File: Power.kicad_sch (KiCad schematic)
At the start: 9 parts, among them U1 CN3063, U3 TPS7A0522PDBV

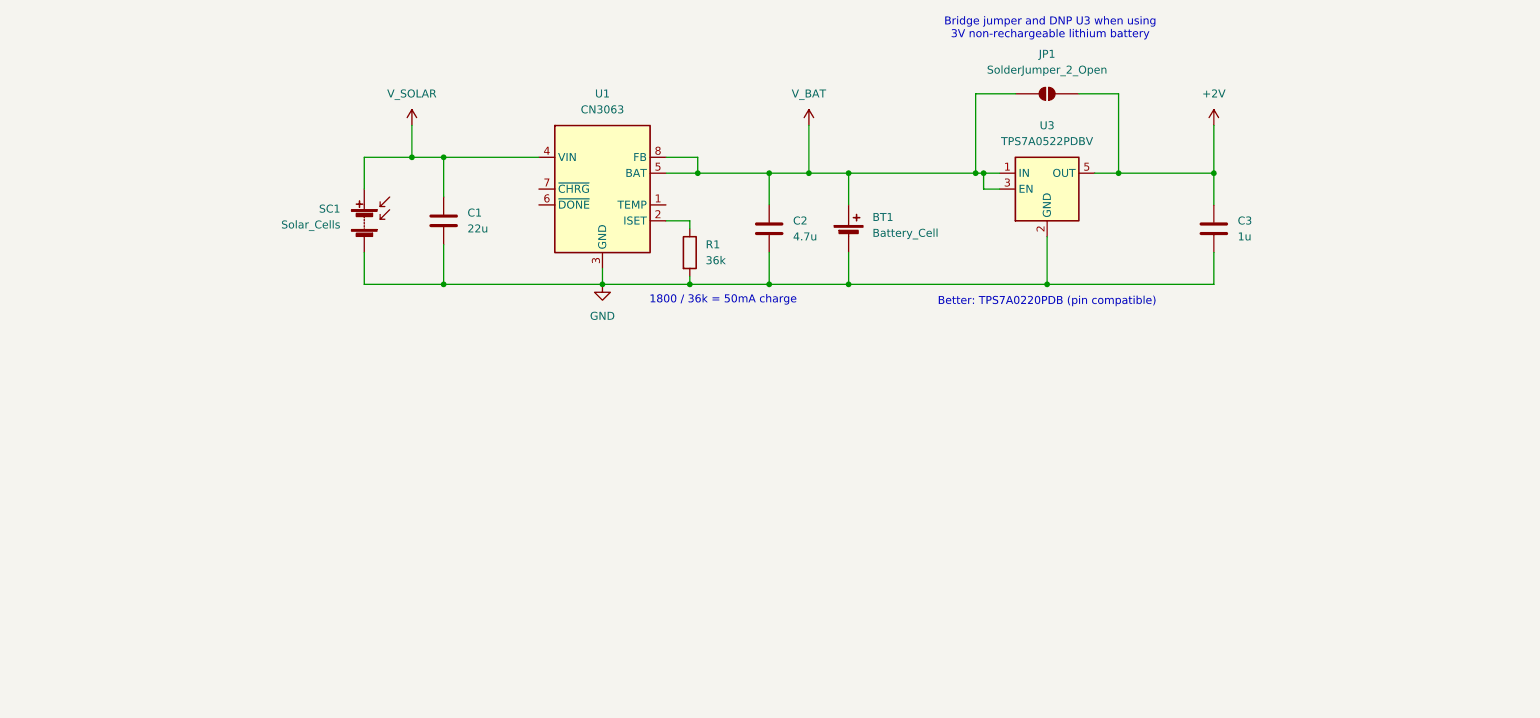
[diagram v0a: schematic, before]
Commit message: add initial pinouts and USB
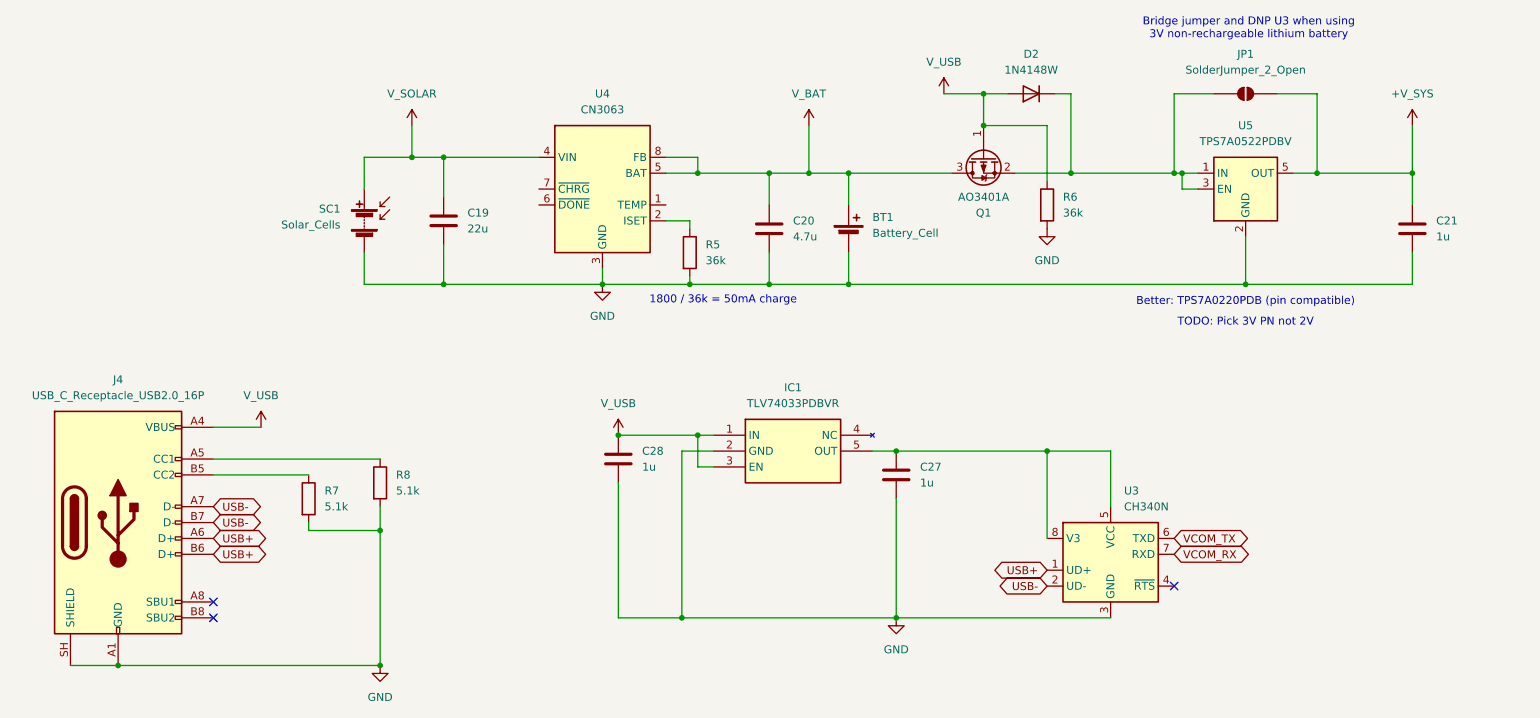
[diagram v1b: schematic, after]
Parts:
- added C27, C28: 1u, Capacitor_SMD:C_0805_2012Metric_Pad1.18x1.45mm_HandSolder, symbol Device:C
- added D2: 1N4148W, Diode_SMD:D_SOD-123, symbol Diode:1N4148W
- added IC1: TLV74033PDBVR, SOT95P280X145-5N, symbol SamacSys_Parts:TLV74033PDBVR
- added J4: USB_C_Receptacle_USB2.0_16P, symbol Connector:USB_C_Receptacle_USB2.0_16P
- added Q1: AO3401A, Package_TO_SOT_SMD:SOT-23, symbol Transistor_FET:AO3401A
- added R6: 36k, Resistor_SMD:R_0603_1608Metric_Pad0.98x0.95mm_HandSolder, symbol Device:R
- added R7, R8: 5.1k, Resistor_SMD:R_0603_1608Metric_Pad0.98x0.95mm_HandSolder, symbol Device:R
- added U3: CH340N, Package_SO:JEITA_SOIC-8_3.9x4.9mm_P1.27mm, symbol Interface_USB:CH340N
- renumbered C1 to C19, C2 to C20, C3 to C21, R1 to R5, U1 to U4, U3 to U5
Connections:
- net GND: now also C27.2, C28.2, IC1.2 (GND), J4.A1 (GND), J4.A12 (GND), J4.B1 (GND), J4.B12 (GND), J4.SH (SHIELD), R6.2, R7.2, R8.2, U3.3 (GND)
- net V_BAT: now also Q1.3 (D); no longer JP1.1 (A), U5.1 (IN), U5.3 (EN)
- net +2V renamed +V_SYS
- new net: C27.1, IC1.5 (OUT), U3.5 (VCC), U3.8 (V3)
- new net: J4.B5 (CC2), R7.1
- new net: D2.1 (K), JP1.1 (A), Q1.2 (S), U5.1 (IN), U5.3 (EN)
- new net: J4.A5 (CC1), R8.1
- new net USB+: J4.A6 (D+), J4.B6 (D+), U3.1 (UD+)
- new net USB-: J4.A7 (D-), J4.B7 (D-), U3.2 (UD-)
- new net VCOM_RX: U3.7 (RXD)
- new net VCOM_TX: U3.6 (TXD)
- new net V_USB: C28.1, D2.2 (A), IC1.1 (IN), IC1.3 (EN), J4.A4 (VBUS), J4.A9 (VBUS), J4.B4 (VBUS), J4.B9 (VBUS), Q1.1 (G), R6.1
- no-connect marks 0 -> 3
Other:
- note added: "TODO: Pick 3V PN not 2V"
- moved on the sheet: C21, JP1, U5

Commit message: add IO ports, begin layout
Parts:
- J4: footprint (none) -> Connector_USB:USB_C_Receptacle_GCT_USB4105-xx-A_16P_TopMnt_Horizontal
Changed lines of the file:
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@@
 			)
 		)
-		(property "Footprint" ""
+		(property "Footprint" "Connector_USB:USB_C_Receptacle_GCT_USB4105-xx-A_16P_TopMnt_Horizontal"
 			(at 49.53 127 0)
 			(hide yes)
@@
 			(at 45.72 127 0)
 			(hide yes)
+			(show_name no)
+			(do_not_autoplace no)
+			(effects
+				(font
+					(size 1.27 1.27)
+				)
+			)
+		)
+		(property "Field5" ""
+			(at 45.72 127 0)
+			(hide yes)

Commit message: minor schematic changes
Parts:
- C21, C27, C28: footprint Capacitor_SMD:C_0805_2012Metric_Pad1.18x1.45mm_HandSolder -> Capacitor_SMD:C_0603_1608Metric_Pad1.08x0.95mm_HandSolder
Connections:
- net V_USB: now also C27.1; no longer C28.1
- net at IC1.5 (OUT), U3.5 (VCC), U3.8 (V3): now also C28.1; no longer C27.1

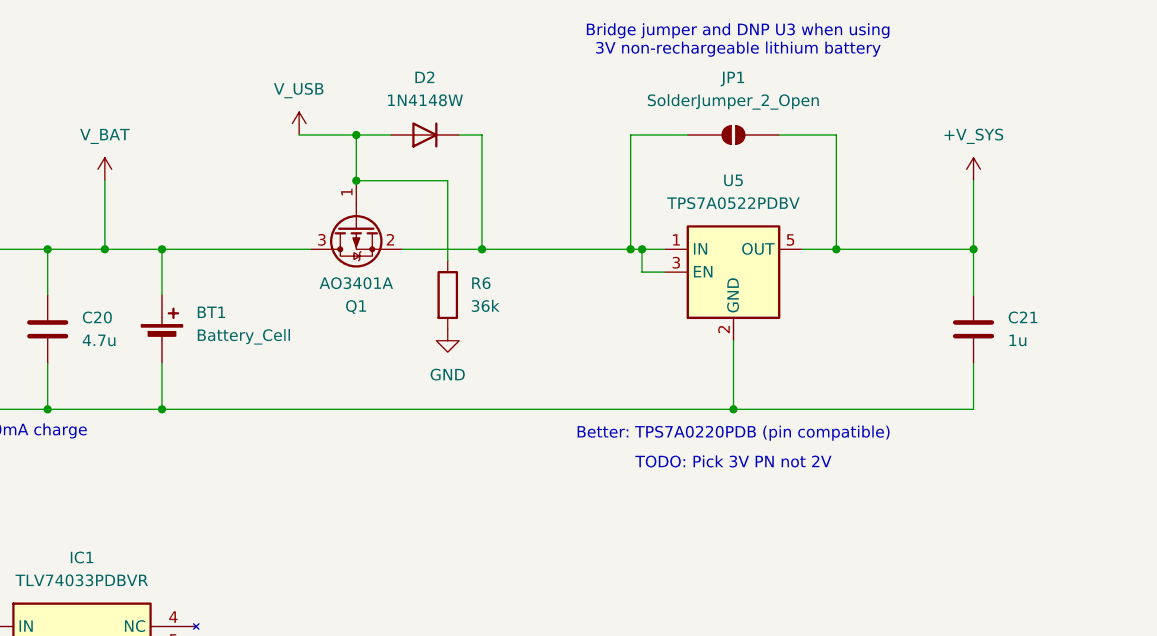
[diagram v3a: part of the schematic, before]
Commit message: initial layout and dense routing near chip
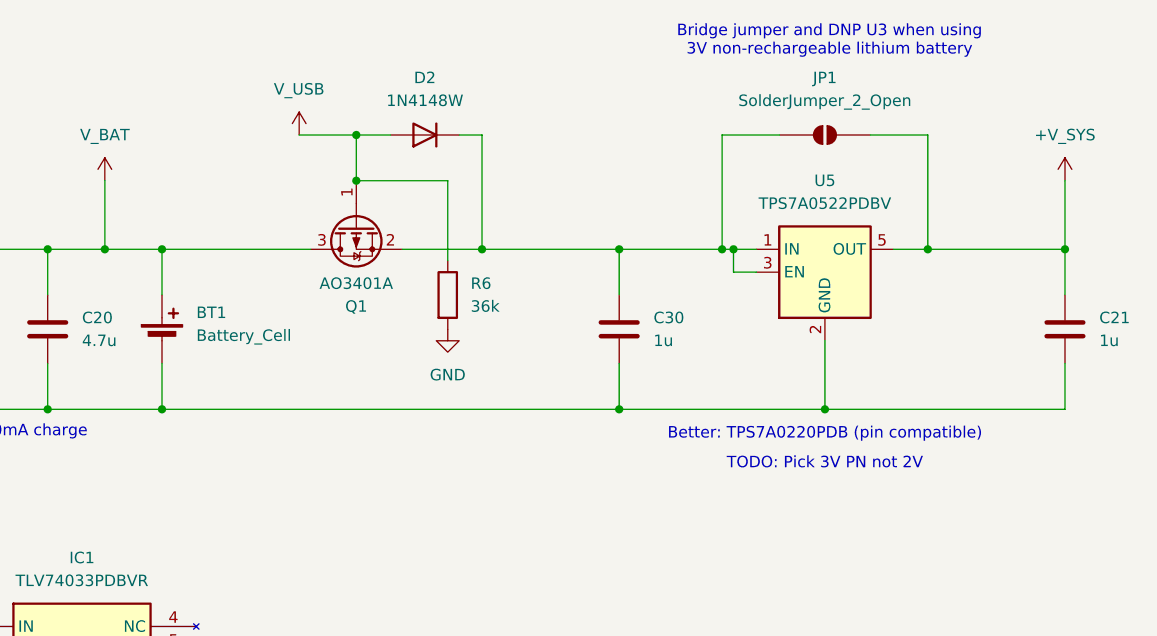
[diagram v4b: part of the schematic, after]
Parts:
- added C30: 1u, Capacitor_SMD:C_0603_1608Metric_Pad1.08x0.95mm_HandSolder, symbol Device:C
- SC1: footprint (none) -> Connector_JST:JST_XH_B2B-XH-AM_1x02_P2.50mm_Vertical
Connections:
- net GND: now also C30.2
- net at D2.1 (K), JP1.1 (A), Q1.2 (S)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: now also C30.1
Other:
- moved on the sheet: C21, JP1, U5

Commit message: minor layout tweaks, add external power header
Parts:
- added J9: Conn_01x02, Connector_PinHeader_2.54mm:PinHeader_1x02_P2.54mm_Vertical, symbol Connector_Generic:Conn_01x02
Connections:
- net GND: now also J9.1 (Pin_1)
- net V_BAT: now also J9.2 (Pin_2)
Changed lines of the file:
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@@
+	)
+	(junction
+		(at 175.26 71.12)
+		(diameter 0)
+		(color 0 0 0 0)
 	)
 	(junction
@@
 	(junction
 		(at 184.15 63.5)
+		(diameter 0)
+		(color 0 0 0 0)
+	)
+	(junction
+		(at 177.8 88.9)
 		(diameter 0)
 		(color 0 0 0 0)
@@
 	(wire
 		(pts
+			(xy 175.26 71.12) (xy 179.07 71.12)
+		)
+		(stroke
+			(width 0)
+			(type default)
+		)
+	)
+	(wire
+		(pts
 			(xy 97.79 68.58) (xy 113.03 68.58)
 		)
@@
 	(wire
 		(pts
+			(xy 177.8 88.9) (xy 162.56 88.9)
+		)
+		(stroke
+			(width 0)
+			(type default)
+		)
+	)
+	(wire
+		(pts
 			(xy 135.89 115.57) (xy 135.89 142.24)
 		)
@@
 	(wire
 		(pts
+			(xy 177.8 88.9) (xy 177.8 93.98)
+		)
+		(stroke
+			(width 0)
+			(type default)
+		)
+	)
+	(wire
+		(pts
 			(xy 92.71 68.58) (xy 97.79 68.58)
 		)
@@
 	(wire
 		(pts
+			(xy 175.26 71.12) (xy 175.26 93.98)
+		)
+		(stroke
+			(width 0)
+			(type default)
+		)
+	)
+	(wire
+		(pts
 			(xy 60.96 116.84) (xy 87.63 116.84)
 		)
@@
 	(wire
 		(pts
-			(xy 162.56 71.12) (xy 179.07 71.12)
+			(xy 162.56 71.12) (xy 175.26 71.12)
 		)
 		(stroke
@@
 	(wire
 		(pts
-			(xy 213.36 88.9) (xy 162.56 88.9)
+			(xy 213.36 88.9) (xy 177.8 88.9)
 		)
 		(stroke
@@
 					(unit 1)
 				)
+			)
+		)
+	)
+	(symbol
+		(lib_id "Connector_Generic:Conn_01x02")
+		(at 177.8 99.06 270)
+		(unit 1)
+		(body_style 1)
+		(exclude_from_sim no)
+		(in_bom yes)
+		(on_board yes)
+		(in_pos_files yes)
+		(dnp no)
+		(fields_autoplaced yes)
+		(property "Reference" "J9"
+			(at 180.34 97.7899 90)
+			(show_name no)
+			(do_not_autoplace no)
+			(effects
+				(font
+					(size 1.27 1.27)
+				)
+				(justify left)
+			)
+		)
+		(property "Value" "Conn_01x02"
+			(at 180.34 100.3299 90)
+			(show_name no)
+			(do_not_autoplace no)
+			(effects
+				(font
+					(size 1.27 1.27)
+				)
+				(justify left)
+			)
+		)
+		(property "Footprint" "Connector_PinHeader_2.54mm:PinHeader_1x02_P2.54mm_Vertical"
+			(at 177.8 99.06 0)
+			(hide yes)
+			(show_name no)
+			(do_not_autoplace no)
+			(effects
+				(font
+					(size 1.27 1.27)
+				)
+			)
+		)
+		(property "Datasheet" ""
+			(at 177.8 99.06 0)
+			(hide yes)
+			(show_name no)
+			(do_not_autoplace no)
+			(effects
+				(font
+					(size 1.27 1.27)
+				)
+			)
+		)
+		(property "Description" "Generic connector, single row, 01x02, script generated (kicad-library-utils/schlib/autogen/connector/)"
+			(at 177.8 99.06 0)
+			(hide yes)
+			(show_name no)
+			(do_not_autoplace no)
+			(effects
+				(font
+					(size 1.27 1.27)
+				)
+			)
+		)
+		(pin "1"
+		)
+		(pin "2"
+		)
+		(instances
+			(project "WINLAB-LP-Radio-Sensor-Hub"
+				(path "/0de7ee4a-bb98-4bc6-bb89-3afafc4b94b5/5ad374ff-424f-46b2-9f18-b4cecbd24790"
+					(reference "J9")
+					(unit 1)
+				)
